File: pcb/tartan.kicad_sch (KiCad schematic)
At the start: 169 parts, among them J1 AVR_ISP_6, J2 USB_OTG, SW1 SW_Push, SW10 SW_Push, SW11 SW_Push, SW12 SW_Push, SW13 SW_Push, SW14 SW_Push, SW15 SW_Push, SW16 SW_Push, SW17 SW_Push, SW18 SW_Push, SW19 SW_Push, SW2 SW_Push, SW20 SW_Push, SW21 SW_Push, SW22 SW_Push, SW23 SW_Push, SW24 SW_Push, SW25 SW_Push, SW26 SW_Push, SW27 SW_Push, SW28 SW_Push, SW29 SW_Push, SW3 SW_Push, SW30 SW_Push, SW31 SW_Push, SW32 SW_Push, SW33 SW_Push, SW34 SW_Push, SW35 SW_Push, SW36 SW_Push, SW37 SW_Push, SW38 SW_Push, SW39 SW_Push, SW4 SW_Push, SW40 SW_Push, SW41 SW_Push, SW42 SW_Push, SW43 SW_Push, SW44 SW_Push, SW45 SW_Push, SW46 SW_Push, SW47 SW_Push, SW48 SW_Push, SW49 SW_Push, SW5 SW_Push, SW50 SW_Push, SW51 SW_Push, SW52 SW_Push, SW53 SW_Push, SW54 SW_Push, SW55 SW_Push, SW56 SW_Push, SW57 SW_Push, SW58 SW_Push, SW59 SW_Push, SW6 SW_Push, SW60 SW_Push, SW61 SW_Push, SW62 SW_Push, SW63 SW_Push, SW64 SW_Push, SW65 SW_Push, SW66 SW_Push, SW67 SW_Push, SW68 SW_Push, SW69 SW_Push, SW7 SW_Push, SW70 RESET, SW71 BOOT, SW8 SW_Push, SW9 SW_Push, U1 ATMEGA328-PU, Y1 16MHz

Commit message: Updated to use new footprints, removed backups directory, as well as specifically removed bottom PCB for sanity savings.
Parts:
- added J3: Conn_01x01_Pin, tartan:bottom1_mask, symbol Connector:Conn_01x01_Pin
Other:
- note added: "Tartan Back Graphic"
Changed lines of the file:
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@@
     (stroke (width 0) (type default))
   )
+  (polyline (pts (xy 298.45 50.8) (xy 299.72 50.8))
+    (stroke (width 0) (type default))
+  )
   (wire (pts (xy 62.23 222.25) (xy 74.93 222.25))
     (stroke (width 0) (type default))
@@
     (stroke (width 0) (type default))
   )
+  (polyline (pts (xy 248.92 50.8) (xy 298.45 50.8))
+    (stroke (width 0) (type default))
+  )
   (wire (pts (xy 222.25 176.53) (xy 222.25 186.69))
     (stroke (width 0) (type default))
@@
     (stroke (width 0) (type default))
   )
+  (rectangle (start 247.65 48.26) (end 300.355 81.28)
+    (stroke (width 0) (type default))
+    (fill (type none))
+  )
   (rectangle (start 203.835 58.42) (end 245.745 90.17)
     (stroke (width 0) (type default))
@@
     (effects (font (size 1.27 1.27)))
   )
+  (text "Tartan Back Graphic" (exclude_from_sim no)
+ (at 258.445 50.165 0)
+    (effects (font (size 1.27 1.27)))
+  )
   (text "Key Matrix" (exclude_from_sim no)
  (at 20.955 116.205 0)
@@
         )
       )
+    )
+  )
+  (symbol (lib_id "Connector:Conn_01x01_Pin") (at 274.32 67.31 0) (unit 1)
+    (exclude_from_sim no) (in_bom yes) (on_board yes) (dnp no) (fields_autoplaced)
+    (property "Reference" "J3" (at 274.955 62.23 0)
+      (effects (font (size 1.27 1.27)))
+    )
+    (property "Value" "Conn_01x01_Pin" (at 274.955 64.77 0)
+      (effects (font (size 1.27 1.27)))
+    )
+    (property "Footprint" "tartan:bottom1_mask" (at 274.32 67.31 0)
+      (effects (font (size 1.27 1.27)) hide)
+    )
+    (property "Datasheet" "~" (at 274.32 67.31 0)
+      (effects (font (size 1.27 1.27)) hide)
+    )
+    (property "Description" "Generic connector, single row, 01x01, script generated" (at 274.32 67.31 0)
+      (effects (font (size 1.27 1.27)) hide)
+    )
+    (pin "1")
+    (instances
+      (project "tartan"
+        (path "/bf5361b0-41e6-43cb-af48-fd796b6d946a"
+          (reference "J3") (unit 1)
+        )
+      )

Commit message: Small cleanup in latest nightly to hopefully minimize truly broken traces.
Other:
- note added: "Questionable Danger Zone!?"
- moved on the sheet: J3
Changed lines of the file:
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@@
     (stroke (width 0) (type default))
   )
-  (polyline (pts (xy 298.45 50.8) (xy 299.72 50.8))
-    (stroke (width 0) (type default))
-  )
   (wire (pts (xy 62.23 222.25) (xy 74.93 222.25))
     (stroke (width 0) (type default))
@@
     (stroke (width 0) (type default))
   )
+  (polyline (pts (xy 349.885 118.745) (xy 386.715 118.745))
+    (stroke (width 0) (type default))
+  )
   (wire (pts (xy 153.67 232.41) (xy 153.67 204.47))
     (stroke (width 0) (type default))
@@
     (stroke (width 0) (type default))
   )
-  (polyline (pts (xy 248.92 50.8) (xy 298.45 50.8))
+  (polyline (pts (xy 248.92 50.8) (xy 288.29 50.8))
     (stroke (width 0) (type default))
   )
@@
     (stroke (width 0) (type default))
   )
-  (rectangle (start 247.65 48.26) (end 300.355 81.28)
+  (rectangle (start 247.65 48.26) (end 288.925 81.28)
     (stroke (width 0) (type default))
     (fill (type none))
@@
     (fill (type none))
   )
+  (rectangle (start 349.25 116.205) (end 387.35 153.67)
+    (stroke (width 0) (type default))
+    (fill (type none))
+  )
   (rectangle (start 247.015 14.605) (end 288.925 46.355)
     (stroke (width 0) (type default))
     (fill (type none))
   )
-  (text_box "Some clever overlapping footprint design permit SW29 and SW66 to share a pad, but this means that in practicality they're \"missing\" on in the DRC."
+  (text_box "Some clever overlapping footprint design permit SW29 and SW66 to share a pad, but this means that in practicality they're \"missing\" on in the DRC.\n\nThis is annoying, but such is life."
     (exclude_from_sim no) (at 205.74 198.755 0) (size 34.925 18.415)
     (stroke (width 0) (type default))
     (fill (type none))
-    (effects (font (size 1.27 1.27)) (justify left top))
+    (effects (font (size 1.27 1.27) (thickness 0.254) bold) (justify left top))
   )
   (text "Decoupling Capacitors for 328p" (exclude_from_sim no)
@@
     (effects (font (size 1.27 1.27)))
   )
+  (text "Questionable Danger Zone!?" (exclude_from_sim no)
+ (at 363.855 118.11 0)
+    (effects (font (size 1.27 1.27)))
+  )
   (text "16MHz Oscillator" (exclude_from_sim no)
  (at 153.035 40.005 0)
@@
     )
   )
-  (symbol (lib_id "mechanical:MountingHole") (at 325.12 58.42 0) (unit 1)
+  (symbol (lib_id "mechanical:MountingHole") (at 360.68 132.08 0) (unit 1)
     (exclude_from_sim no) (in_bom yes) (on_board yes) (dnp no)
-    (property "Reference" "STAB1" (at 327.66 57.2516 0)
+    (property "Reference" "STAB1" (at 363.22 130.9116 0)
       (effects (font (size 1.27 1.27)) (justify left))
     )
-    (property "Value" "2U" (at 327.66 59.563 0)
+    (property "Value" "2U" (at 363.22 133.223 0)
       (effects (font (size 1.27 1.27)) (justify left))
     )
-    (property "Footprint" "SMKJP:Stab_MX_2u" (at 325.12 58.42 0)
+    (property "Footprint" "SMKJP:Stab_MX_2u" (at 360.68 132.08 0)
       (effects (font (size 1.27 1.27)) hide)
     )
-    (property "Datasheet" "~" (at 325.12 58.42 0)
+    (property "Datasheet" "~" (at 360.68 132.08 0)
       (effects (font (size 1.27 1.27)) hide)
     )
-    (property "Description" "" (at 325.12 58.42 0)
+    (property "Description" "" (at 360.68 132.08 0)
       (effects (font (size 1.27 1.27)) hide)
     )
@@
     )
   )
-  (symbol (lib_id "mechanical:MountingHole") (at 340.36 58.42 0) (unit 1)
+  (symbol (lib_id "mechanical:MountingHole") (at 375.92 132.08 0) (unit 1)
     (exclude_from_sim no) (in_bom yes) (on_board yes) (dnp no)
-    (property "Reference" "STAB2" (at 342.9 57.2516 0)
+    (property "Reference" "STAB2" (at 378.46 130.9116 0)
       (effects (font (size 1.27 1.27)) (justify left))
     )
-    (property "Value" "2U" (at 342.9 59.563 0)
+    (property "Value" "2U" (at 378.46 133.223 0)
       (effects (font (size 1.27 1.27)) (justify left))
     )
-    (property "Footprint" "SMKJP:Stab_MX_2u" (at 340.36 58.42 0)
+    (property "Footprint" "SMKJP:Stab_MX_2u" (at 375.92 132.08 0)
       (effects (font (size 1.27 1.27)) hide)
     )
-    (property "Datasheet" "~" (at 340.36 58.42 0)
+    (property "Datasheet" "~" (at 375.92 132.08 0)
       (effects (font (size 1.27 1.27)) hide)
     )
-    (property "Description" "" (at 340.36 58.42 0)
+    (property "Description" "" (at 375.92 132.08 0)
       (effects (font (size 1.27 1.27)) hide)
     )
@@
     )
   )
-  (symbol (lib_id "mechanical:MountingHole") (at 325.12 63.5 0) (unit 1)
+  (symbol (lib_id "mechanical:MountingHole") (at 360.68 137.16 0) (unit 1)
     (exclude_from_sim no) (in_bom yes) (on_board yes) (dnp no)
-    (property "Reference" "STAB3" (at 327.66 62.3316 0)
+    (property "Reference" "STAB3" (at 363.22 135.9916 0)
       (effects (font (size 1.27 1.27)) (justify left))
     )
-    (property "Value" "2U" (at 327.66 64.643 0)
+    (property "Value" "2U" (at 363.22 138.303 0)
       (effects (font (size 1.27 1.27)) (justify left))
     )
-    (property "Footprint" "SMKJP:Stab_MX_2u" (at 325.12 63.5 0)
+    (property "Footprint" "SMKJP:Stab_MX_2u" (at 360.68 137.16 0)
       (effects (font (size 1.27 1.27)) hide)
     )
-    (property "Datasheet" "~" (at 325.12 63.5 0)
+    (property "Datasheet" "~" (at 360.68 137.16 0)
       (effects (font (size 1.27 1.27)) hide)
     )
-    (property "Description" "" (at 325.12 63.5 0)
+    (property "Description" "" (at 360.68 137.16 0)
       (effects (font (size 1.27 1.27)) hide)
     )
@@
     )
   )
-  (symbol (lib_id "mechanical:MountingHole") (at 340.36 63.5 0) (unit 1)
+  (symbol (lib_id "mechanical:MountingHole") (at 375.92 137.16 0) (unit 1)
     (exclude_from_sim no) (in_bom yes) (on_board yes) (dnp no)
-    (property "Reference" "STAB4" (at 342.9 62.3316 0)
+    (property "Reference" "STAB4" (at 378.46 135.9916 0)
       (effects (font (size 1.27 1.27)) (justify left))
     )
-    (property "Value" "2U" (at 342.9 64.643 0)
+    (property "Value" "2U" (at 378.46 138.303 0)
       (effects (font (size 1.27 1.27)) (justify left))
     )
-    (property "Footprint" "SMKJP:Stab_MX_2u" (at 340.36 63.5 0)
+    (property "Footprint" "SMKJP:Stab_MX_2u" (at 375.92 137.16 0)
       (effects (font (size 1.27 1.27)) hide)
     )
-    (property "Datasheet" "~" (at 340.36 63.5 0)
+    (property "Datasheet" "~" (at 375.92 137.16 0)
       (effects (font (size 1.27 1.27)) hide)
     )
-    (property "Description" "" (at 340.36 63.5 0)
+    (property "Description" "" (at 375.92 137.16 0)
       (effects (font (size 1.27 1.27)) hide)
     )
@@
     )
   )
-  (symbol (lib_id "mechanical:MountingHole") (at 325.12 68.58 0) (unit 1)
+  (symbol (lib_id "mechanical:MountingHole") (at 360.68 142.24 0) (unit 1)
     (exclude_from_sim no) (in_bom yes) (on_board yes) (dnp no)
-    (property "Reference" "STAB5" (at 327.66 67.4116 0)
+    (property "Reference" "STAB5" (at 363.22 141.0716 0)
       (effects (font (size 1.27 1.27)) (justify left))
     )
-    (property "Value" "2U" (at 327.66 69.723 0)
+    (property "Value" "2U" (at 363.22 143.383 0)
       (effects (font (size 1.27 1.27)) (justify left))
     )
-    (property "Footprint" "SMKJP:Stab_MX_2u" (at 325.12 68.58 0)
+    (property "Footprint" "SMKJP:Stab_MX_2u" (at 360.68 142.24 0)
       (effects (font (size 1.27 1.27)) hide)
     )
-    (property "Datasheet" "~" (at 325.12 68.58 0)
+    (property "Datasheet" "~" (at 360.68 142.24 0)
       (effects (font (size 1.27 1.27)) hide)
     )
-    (property "Description" "" (at 325.12 68.58 0)
+    (property "Description" "" (at 360.68 142.24 0)
       (effects (font (size 1.27 1.27)) hide)
     )
@@
     )
   )
-  (symbol (lib_id "mechanical:MountingHole") (at 340.36 68.58 0) (unit 1)
+  (symbol (lib_id "mechanical:MountingHole") (at 375.92 142.24 0) (unit 1)
     (exclude_from_sim no) (in_bom yes) (on_board yes) (dnp no)
-    (property "Reference" "STAB6" (at 342.9 67.4116 0)
+    (property "Reference" "STAB6" (at 378.46 141.0716 0)
       (effects (font (size 1.27 1.27)) (justify left))
     )
-    (property "Value" "2U" (at 342.9 69.723 0)
+    (property "Value" "2U" (at 378.46 143.383 0)
       (effects (font (size 1.27 1.27)) (justify left))
     )
-    (property "Footprint" "Button_Switch_Keyboard:SW_Cherry_MX1A_6.25u_PCB" (at 340.36 68.58 0)
+    (property "Footprint" "Button_Switch_Keyboard:SW_Cherry_MX1A_6.25u_PCB" (at 375.92 142.24 0)
       (effects (font (size 1.27 1.27)) hide)
     )
-    (property "Datasheet" "~" (at 340.36 68.58 0)
+    (property "Datasheet" "~" (at 375.92 142.24 0)
       (effects (font (size 1.27 1.27)) hide)
     )
-    (property "Description" "" (at 340.36 68.58 0)
+    (property "Description" "" (at 375.92 142.24 0)
       (effects (font (size 1.27 1.27)) hide)
     )
@@
     )
   )
-  (symbol (lib_id "Connector:Conn_01x01_Pin") (at 274.32 67.31 0) (unit 1)
+  (symbol (lib_id "Connector:Conn_01x01_Pin") (at 267.97 68.58 0) (unit 1)
     (exclude_from_sim no) (in_bom yes) (on_board yes) (dnp no) (fields_autoplaced)
-    (property "Reference" "J3" (at 274.955 62.23 0)
+    (property "Reference" "J3" (at 268.605 63.5 0)
       (effects (font (size 1.27 1.27)))
     )
-    (property "Value" "Conn_01x01_Pin" (at 274.955 64.77 0)
+    (property "Value" "Conn_01x01_Pin" (at 268.605 66.04 0)
       (effects (font (size 1.27 1.27)))
     )
-    (property "Footprint" "tartan:bottom1_mask" (at 274.32 67.31 0)
+    (property "Footprint" "tartan:bottom1_mask" (at 267.97 68.58 0)
       (effects (font (size 1.27 1.27)) hide)
     )
-    (property "Datasheet" "~" (at 274.32 67.31 0)
+    (property "Datasheet" "~" (at 267.97 68.58 0)
       (effects (font (size 1.27 1.27)) hide)
     )
-    (property "Description" "Generic connector, single row, 01x01, script generated" (at 274.32 67.31 0)
+    (property "Description" "Generic connector, single row, 01x01, script generated" (at 267.97 68.58 0)
       (effects (font (size 1.27 1.27)) hide)
     )

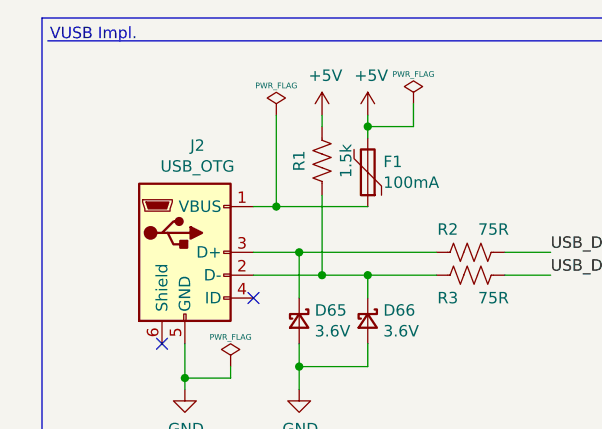
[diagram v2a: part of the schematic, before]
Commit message: Update to new USB B that Ben found.
	new file:   pcb/sym-lib-table
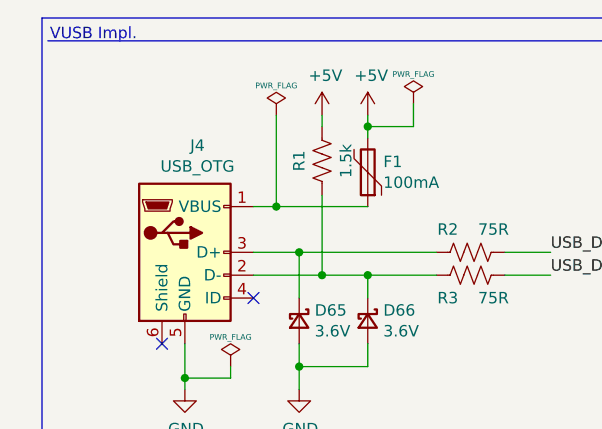
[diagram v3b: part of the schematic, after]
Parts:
- removed J2: USB_OTG, tartan:USB_MINIB_Akizuki_MUSB-5BF01AS, symbol Connector:USB_OTG
- added J4: USB_OTG, tartan:USB B THT 1734510-1_TEC, symbol Connector:USB_OTG
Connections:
- net GND: now also J4.5 (GND)
- net at D65.1 (K), R2.2: now also J4.3 (D+)
- net at D66.1 (K), R1.1, R3.2: now also J4.2 (D-)
- net at F1.1: now also J4.1 (VBUS)
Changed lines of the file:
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@@
-    )
-  )
-  (symbol (lib_id "Connector:USB_OTG") (at 30.48 40.64 0) (unit 1)
-    (exclude_from_sim no) (in_bom yes) (on_board yes) (dnp no)
-    (property "Reference" "J2" (at 31.877 28.7782 0)
-      (effects (font (size 1.27 1.27)))
-    )
-    (property "Value" "USB_OTG" (at 31.877 31.0896 0)
-      (effects (font (size 1.27 1.27)))
-    )
-    (property "Footprint" "tartan:USB_MINIB_Akizuki_MUSB-5BF01AS" (at 34.29 41.91 0)
-      (effects (font (size 1.27 1.27)) hide)
-    )
-    (property "Datasheet" " ~" (at 34.29 41.91 0)
-      (effects (font (size 1.27 1.27)) hide)
-    )
-    (property "Description" "USB mini/micro connector" (at 30.48 40.64 0)
-      (effects (font (size 1.27 1.27)) hide)
-    )
-    (pin "6")
-    (pin "4")
-    (pin "2")
-    (pin "3")
-    (pin "5")
-    (pin "1")
-    (instances
-      (project "tartan"
-        (path "/bf5361b0-41e6-43cb-af48-fd796b6d946a"
-          (reference "J2") (unit 1)
-        )
-      )
     )
   )
@@
         )
       )
+    )
+  )
+  (symbol (lib_id "Connector:USB_OTG") (at 30.48 40.64 0) (unit 1)
+    (exclude_from_sim no) (in_bom yes) (on_board yes) (dnp no)
+    (property "Reference" "J4" (at 31.877 28.7782 0)
+      (effects (font (size 1.27 1.27)))
+    )
+    (property "Value" "USB_OTG" (at 31.877 31.0896 0)
+      (effects (font (size 1.27 1.27)))
+    )
+    (property "Footprint" "tartan:USB B THT 1734510-1_TEC" (at 34.29 41.91 0)
+      (effects (font (size 1.27 1.27)) hide)
+    )
+    (property "Datasheet" " ~" (at 34.29 41.91 0)
+      (effects (font (size 1.27 1.27)) hide)
+    )
+    (property "Description" "USB mini/micro connector" (at 30.48 40.64 0)
+      (effects (font (size 1.27 1.27)) hide)
+    )
+    (pin "6")
+    (pin "4")
+    (pin "2")
+    (pin "3")
+    (pin "5")
+    (pin "1")
+    (instances
+      (project "tartan"
+        (path "/bf5361b0-41e6-43cb-af48-fd796b6d946a"
+          (reference "J4") (unit 1)
+        )
+      )

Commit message: Added stabilizers back and hopefully fixed a bunch of issues (tm).
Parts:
- STAB1, STAB2, STAB3, STAB4, STAB5: footprint SMKJP:Stab_MX_2u -> tartan:STAB_MX_2u; symbol mechanical:MountingHole -> Mechanical:MountingHole
- STAB6: value 2U -> 6.25u; footprint Button_Switch_Keyboard:SW_Cherry_MX1A_6.25u_PCB -> tartan:STAB_MX_6.25u; symbol mechanical:MountingHole -> Mechanical:MountingHole
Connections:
- net D+: now reaches D65.1 (K), J4.3 (D+), R2.2
- net D-: now reaches D66.1 (K), J4.2 (D-), R1.1, R3.2
